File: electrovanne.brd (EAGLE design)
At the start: 44.1 x 91 mm, 17 parts, among them IC1 7805TV, T1 2N2222, T2 2N2222, X1 MKDSN1,5/2-5,08

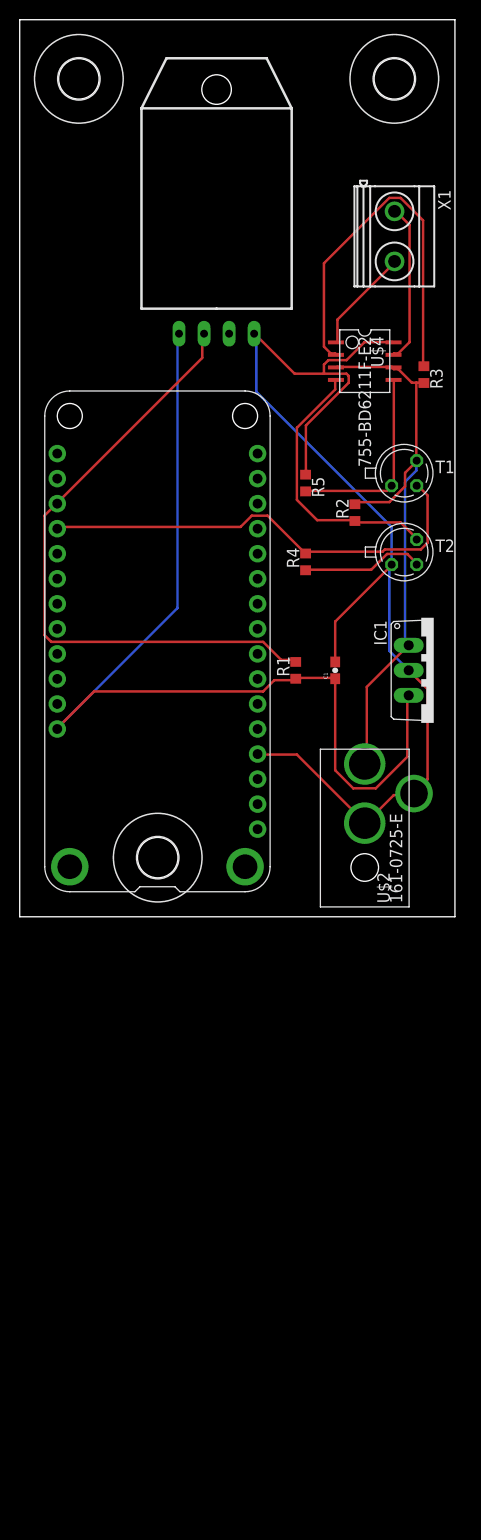
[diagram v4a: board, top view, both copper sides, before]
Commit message: version 3: pb wit the RIN inverter
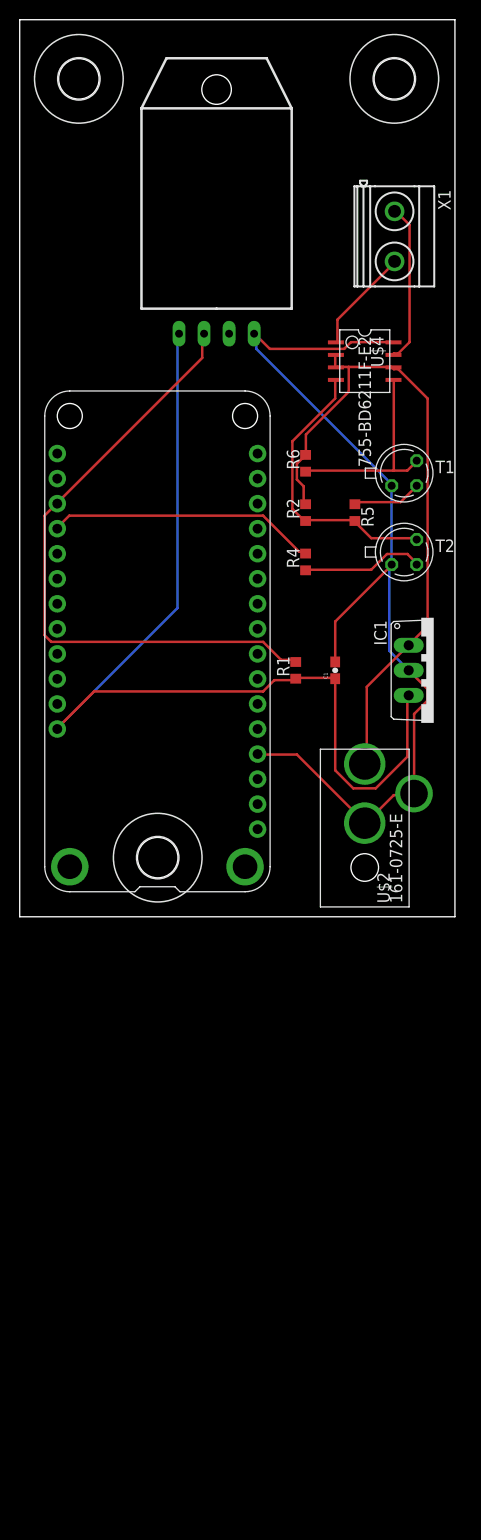
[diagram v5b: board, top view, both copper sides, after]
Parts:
- removed R3: 10, resistor:R0603
- added R6: 10k, resistor:R0603
- R2: value 10k -> 1k
- moved R5 5.83 mm to (34.0, 41.0)
- moved R2 5.00 mm to (29.0, 41.0)
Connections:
- removed net N$5: R3.1, U$4.P$2
- new net N$10: R6.1, T1.3, U$4.P$5
- net GND: now also T1.1; no longer R5.1
- net N$1: now also R6.2, U$4.P$2; no longer R3.2, T1.3
- net N$2: now also R5.1, T1.2; no longer R5.2, T1.1, U$4.P$5
- net N$7: no longer T1.2
- net N$8: now also R5.2
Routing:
- net N$5: track 38.6 -> 0.00 mm
- net N$10: track 0.00 -> 21.0 mm
- net N$7: track 46.6 -> 27.4 mm
- net GND: track 119.1 -> 102.0 mm
- net N$2: track 19.9 -> 7.13 mm
- net N$1: track 59.9 -> 68.3 mm
- net N$8: track 27.7 -> 29.0 mm
